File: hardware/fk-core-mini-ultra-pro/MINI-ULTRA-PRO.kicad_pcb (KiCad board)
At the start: 2 copper layers, 25.4 x 55.9 mm, 62 parts, among them J1 S2B-PH-SM4-TB, J2 MICRO-USB, J3 RF-SMA-EDGE, J4 CONN-HDR-1x19, J5 CONN-HDR-1x19, J6 CONN-HDR-2x5, M1 MOUNT_HOLE, M2 MOUNT_HOLE, M3 MOUNT_HOLE, M4 MOUNT_HOLE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

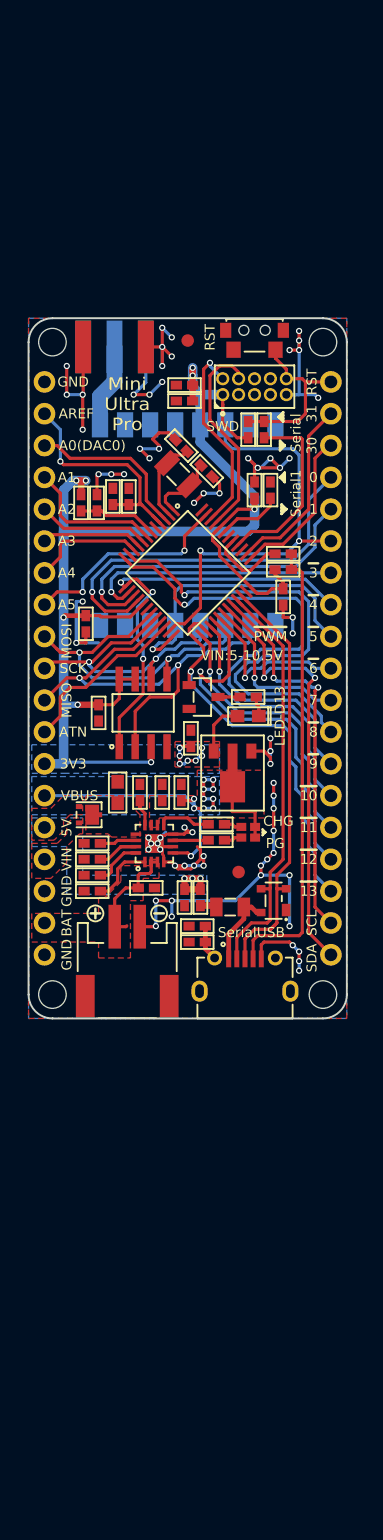
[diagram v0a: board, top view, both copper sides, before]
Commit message: Laying out our additions to the MUP pcb. SD/GPS/Fuel gauge.
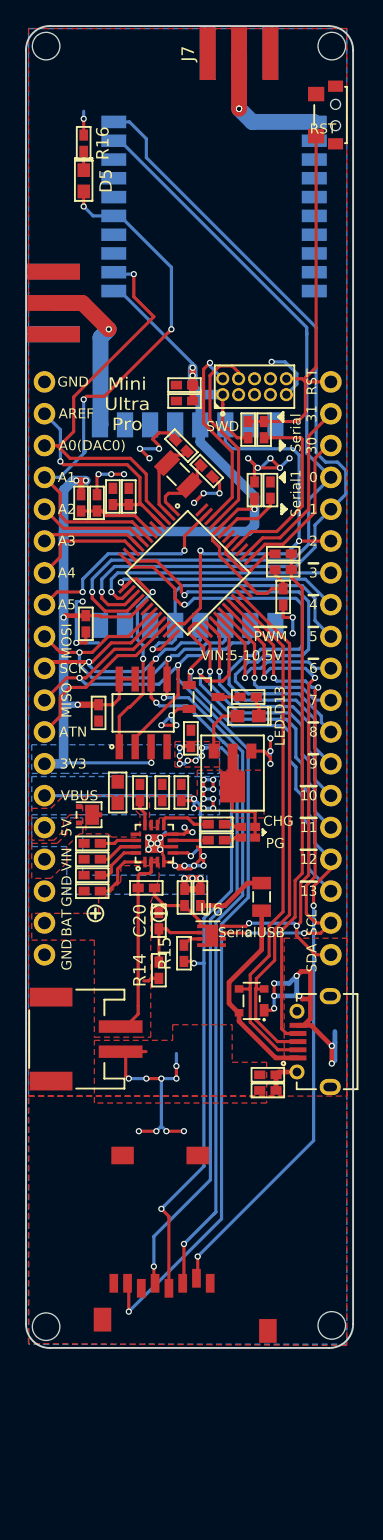
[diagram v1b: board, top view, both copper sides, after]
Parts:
- removed M5, M6: FIDUCIAL, RocketScreamKicadLibrary:FIDUCIAL-1MM
- added C20: 1uF 10V X5R, RocketScreamKicadLibrary:CAP-0402, F.Cu at (137.4, 119.2)
- added D5: Red, RocketScreamKicadLibrary:LED-0603, F.Cu at (131.4, 60.1)
- added J7: RF-SMA-EDGE, RocketScreamKicadLibrary:RF-SMA-EDGE, F.Cu at (143.8, 50.0)
- added M7: MICROSD, microsd:MICROSD, F.Cu at (132.5, 137.5)
- added R14: 1k, RocketScreamKicadLibrary:RES-0402, F.Cu at (137.4, 123.2)
- added R15: 180, RocketScreamKicadLibrary:RES-0402, F.Cu at (139.4, 121.8)
- added R16: 470R, RocketScreamKicadLibrary:RES-0402, F.Cu at (131.4, 57.1)
- added U6: MAX1704XX, Housings_DFN_QFN:DFN-8-1EP_2x2mm_Pitch0.5mm, F.Cu at (141.6, 120.4)
- added U7: FGPMMOPA6H, FGPMMOPA6H:FGPMMOPA6H, B.Cu at (141.8, 62.2)
- J3: moved to F.Cu
- moved M1 26.5 mm to (128.4, 151.6)
- moved M2 26.4 mm to (151.2, 151.5)
- moved M4 23.6 mm to (151.2, 49.4)
- moved M3 23.6 mm to (128.4, 49.4)
- moved SW1 18.2 mm to (151.7, 54.9), turned to 270 degrees
- moved R5 14.3 mm to (146.1, 132.8)
- moved C18 12.0 mm to (146.1, 131.5)
- moved D3 8.19 mm to (144.8, 125.6)
- moved J2 7.67 mm to (149.9, 128.8), turned to 90 degrees
- moved J1 7.03 mm to (131.6, 128.7), turned to 270 degrees
- moved J3 5.99 mm to (129.0, 69.9), turned to 180 degrees
- moved LOGO2 3.06 mm to (136.1, 120.0)
- moved F1 2.64 mm to (145.6, 117.3), turned to 270 degrees
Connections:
- J1 pad 3: Net-(J1-Pad3) -> (no net)
- J1 pad 4: Net-(J1-Pad4) -> (no net)
- J2 pad 7: Net-(J2-Pad7) -> (no net)
- J2 pad 8: Net-(J2-Pad8) -> (no net)
- J2 pad 9: Net-(J2-Pad9) -> (no net)
- J3 pad 2: GND -> (no net)
- J6 pad 6: Net-(J6-Pad6) -> (no net)
- J6 pad 7: Net-(J6-Pad7) -> (no net)
- J6 pad 8: Net-(J6-Pad8) -> (no net)
- U1 pad 39: /TX_LED -> (no net)
- U1 pad 48: /RX_LED -> (no net)
- U3 pad 11: Net-(U3-Pad11) -> (no net)
- U3 pad 12: Net-(U3-Pad12) -> (no net)
- U3 pad 15: Net-(U3-Pad15) -> (no net)
- U3 pad 16: Net-(U3-Pad16) -> (no net)
- U3 pad 6: Net-(U3-Pad6) -> (no net)
- U3 pad 7: Net-(U3-Pad7) -> (no net)
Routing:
- net /MISO: track 37.3 -> 96.4 mm, vias 2 -> 3
- net 3V3: track 130.9 -> 189.9 mm, vias 15 -> 17
- net /SCK: track 23.9 -> 82.3 mm, vias 2 -> 4
- net /MOSI: track 27.5 -> 81.6 mm, vias 2 -> 4
- net /D1: track 26.2 -> 67.1 mm
- net /D12: track 29.3 -> 67.2 mm, vias 1 -> 3
- net /D0: track 30.5 -> 65.0 mm
- net /A1: track 11.2 -> 44.1 mm, vias 0 -> 3
- net /A0: track 13.2 -> 33.6 mm, vias 0 -> 1
- net /RST: track 13.7 -> 31.0 mm
- net Net-(J7-Pad1): track 0.00 -> 10.8 mm, vias 0 -> 2
- net /SCL: track 30.5 -> 40.8 mm, vias 2 -> 4
- net VUSB: track 6.20 -> 16.2 mm
- net GND: track 120.3 -> 111.5 mm, vias 69 -> 55
- net /USB-: track 33.2 -> 41.9 mm
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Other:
- board size 25.4 x 55.9 mm -> 26.1 x 105.5 mm
- net class Default: clearance 0.2032 -> 0.19
- rule trace_clearance: 0.2032 -> 0.19
- rule trace_min: 0.2032 -> 0.19

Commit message: Fixing up edge cuts and consolidating pours.
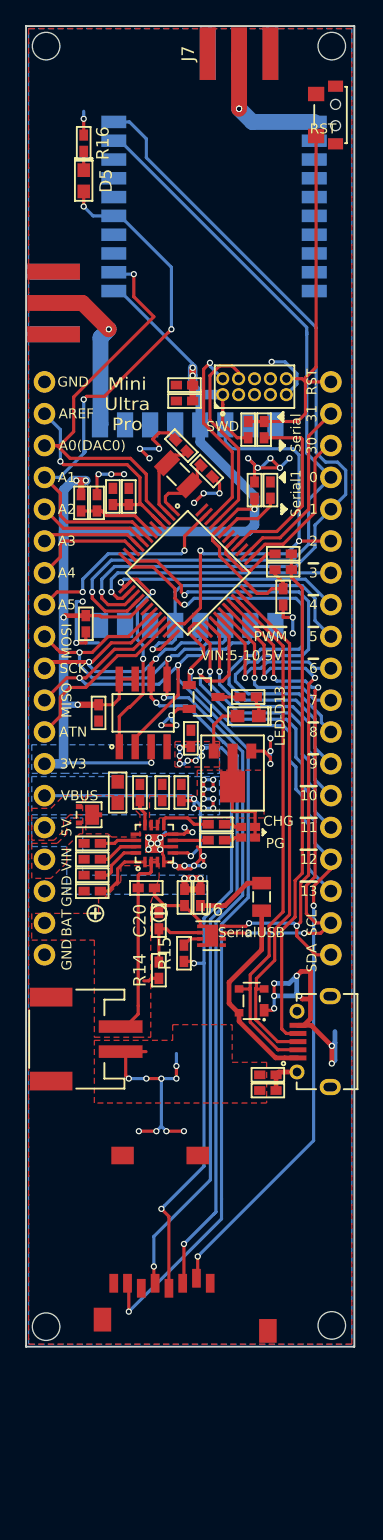
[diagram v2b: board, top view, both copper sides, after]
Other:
- board size 26.1 x 105.5 mm -> 26.2 x 105.4 mm
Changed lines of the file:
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@@
     (links 210)
     (no_connects 0)
-    (area 126.674999 47.744999 152.475001 153.325001)
+    (area 104.521 29.804952 174.451 159.377948)
     (thickness 1.6)
-    (drawings 102)
+    (drawings 98)
     (tracks 1015)
     (zones 0)
@@
     (pad 20 smd rect (at 8.001 6.74878) (size 1.99898 1.00076) (layers B.Cu B.Paste B.Mask))
   )
-  (gr_line (start 126.8 151.4) (end 126.8 49.7) (layer Edge.Cuts) (width 0.15))
-  (gr_line (start 152.9 49.7) (end 152.9 151.4) (layer Edge.Cuts) (width 0.15))
+  (gr_line (start 126.8 153.2) (end 126.8 47.8) (layer Edge.Cuts) (width 0.15))
+  (gr_line (start 153 47.8) (end 153 153.2) (layer Edge.Cuts) (width 0.15))
   (gr_text "Made\nWith" (at 131.572 106.934) (layer B.SilkS)
     (effects (font (size 0.8 0.8) (thickness 0.15)) (justify mirror))
@@
     (effects (font (size 0.8 0.8) (thickness 0.15)))
   )
-  (gr_text RST (at 150.5 56 360) (layer F.SilkS)
+  (gr_text RST (at 150.5 56) (layer F.SilkS)
     (effects (font (size 0.8 0.8) (thickness 0.15)))
   )
@@
   (gr_line (start 131.953 118.618) (end 132.715 118.618) (layer F.SilkS) (width 0.2))
   (gr_line (start 132.334 118.237) (end 132.334 118.999) (layer F.SilkS) (width 0.2))
-  (gr_arc (start 151 151.4) (end 152.905 151.4) (angle 90) (layer Edge.Cuts) (width 0.15))
-  (gr_arc (start 128.7 151.4) (end 128.7 153.305) (angle 90) (layer Edge.Cuts) (width 0.15))
-  (gr_arc (start 150.98 49.73) (end 150.98 47.805) (angle 90.77421614) (layer Edge.Cuts) (width 0.15))
-  (gr_arc (start 128.7 49.7) (end 126.795 49.7) (angle 89.85854995) (layer Edge.Cuts) (width 0.15))
   (gr_text SCL (at 149.606 119.38 90) (layer F.SilkS)
     (effects (font (size 0.8 0.8) (thickness 0.15)))
@@
     (arrow2b (pts (xy 157.35 47.75) (xy 157.936421 48.876504)))
   )
-  (gr_line (start 151 153.3) (end 128.7 153.3) (layer Edge.Cuts) (width 0.15))
-  (gr_line (start 128.7 47.8) (end 151 47.8) (layer Edge.Cuts) (width 0.15))
+  (gr_line (start 153 153.2) (end 126.8 153.2) (layer Edge.Cuts) (width 0.15))
+  (gr_line (start 126.8 47.8) (end 153 47.8) (layer Edge.Cuts) (width 0.15))
   (segment (start 145.376 102.362) (end 145.376 102.87) (width 0.254) (layer F.Cu) (net 1))
   (segment (start 145.376 102.362) (end 145.376 102.108) (width 0.254) (layer F.Cu) (net 1))
@@
     (polygon
       (pts
-        (xy 127 48) (xy 152.4 48) (xy 152.4 153) (xy 127 153)
+        (xy 127 48) (xy 152.8 48) (xy 152.8 153) (xy 127 153)
       )
     )
@@
     (polygon
       (pts
-        (xy 127 48) (xy 127 133.2) (xy 152.4 133.2) (xy 152.4 48)
+        (xy 127 48) (xy 127 153) (xy 152.8 153) (xy 152.8 48)
       )
     )
@@
       )
     )
-  )
-  (zone (net 5) (net_name GND) (layer F.Cu) (hatch edge 0.508)
-    (connect_pads (clearance 0.2032))
-    (min_thickness 0.254)
-    (fill yes (arc_segments 16) (thermal_gap 0.508) (thermal_bridge_width 0.508))
-    (polygon
-      (pts
-        (xy 152.4 153.1) (xy 127 152.95) (xy 127 133.2) (xy 147.4 133.2) (xy 147.4 120.6)
-        (xy 152.4 120.6)
-      )
-    )

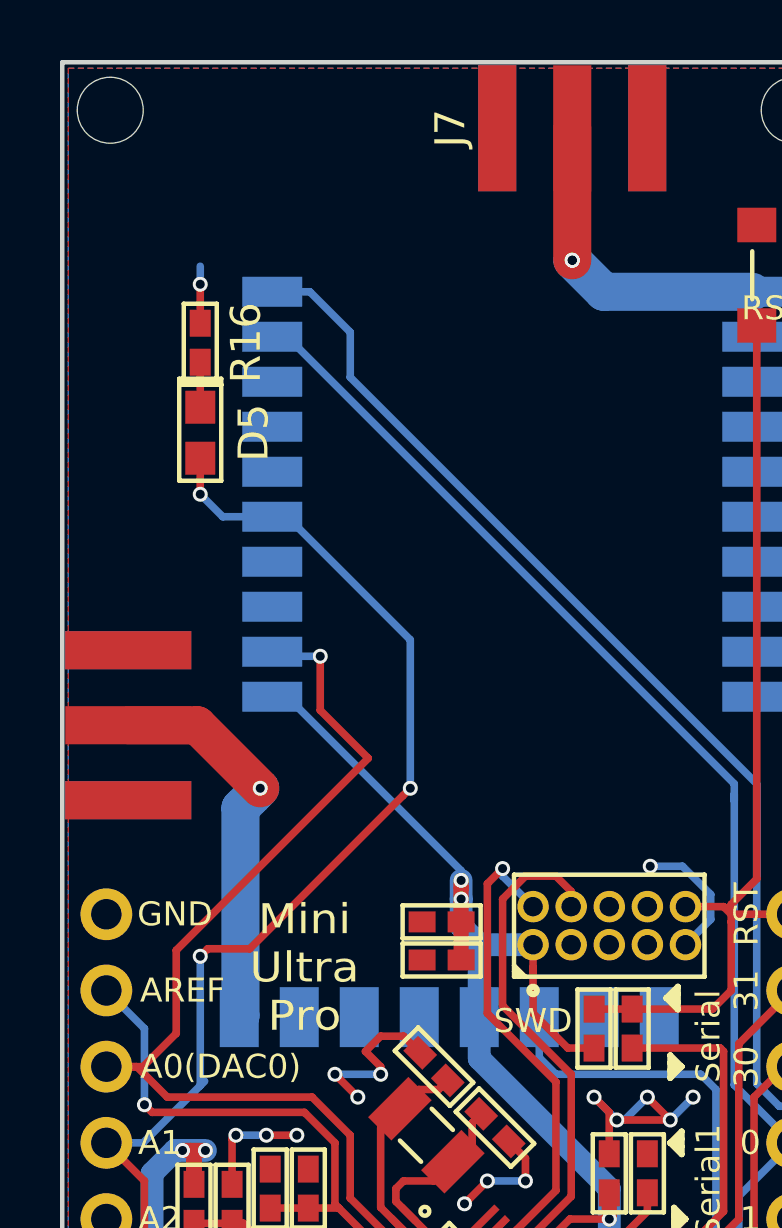
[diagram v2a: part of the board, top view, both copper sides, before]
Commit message: Cleanup silkscreen and some tweaks.
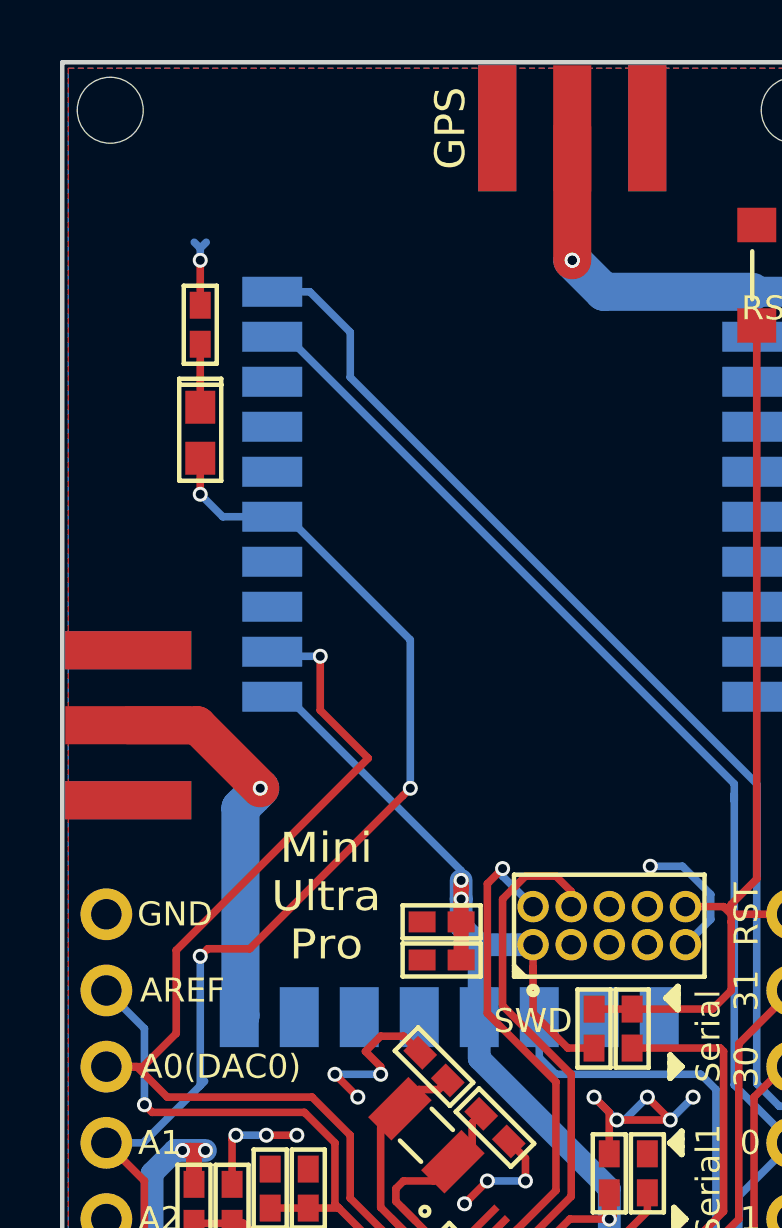
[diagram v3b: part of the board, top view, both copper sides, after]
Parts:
- moved R16 0.60 mm to (131.4, 56.5)
- renumbered J7 to GPS
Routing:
- net Net-(D5-Pad1): track 1.50 -> 2.10 mm
- net GND: track 111.5 -> 112.1 mm
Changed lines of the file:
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@@
     (links 210)
     (no_connects 0)
-    (area 104.521 29.804952 174.451 159.377948)
+    (area 126.724999 47.724999 153.075001 153.275001)
     (thickness 1.6)
     (drawings 98)
-    (tracks 1015)
+    (tracks 1017)
     (zones 0)
     (modules 69)
@@
     (0 F.Cu signal)
     (31 B.Cu signal)
-    (32 B.Adhes user hide)
-    (33 F.Adhes user hide)
-    (34 B.Paste user hide)
-    (35 F.Paste user hide)
+    (32 B.Adhes user)
+    (33 F.Adhes user)
+    (34 B.Paste user)
+    (35 F.Paste user)
     (36 B.SilkS user)
     (37 F.SilkS user)
-    (38 B.Mask user hide)
-    (39 F.Mask user hide)
-    (40 Dwgs.User user)
-    (41 Cmts.User user)
+    (38 B.Mask user)
+    (39 F.Mask user)
+    (40 Dwgs.User user hide)
+    (41 Cmts.User user hide)
     (42 Eco1.User user hide)
     (43 Eco2.User user hide)
     (44 Edge.Cuts user)
     (45 Margin user hide)
-    (46 B.CrtYd user hide)
-    (47 F.CrtYd user hide)
-    (48 B.Fab user)
-    (49 F.Fab user)
+    (46 B.CrtYd user)
+    (47 F.CrtYd user)
+    (48 B.Fab user hide)
+    (49 F.Fab user hide)
   )
   (setup
@@
     (aux_axis_origin 127 127)
     (grid_origin 127 127)
-    (visible_elements 7FFCDF19)
+    (visible_elements 7FFFDF7F)
     (pcbplotparams
       (layerselection 0x010fc_80000001)
@@
     (tags "LED led 0603 SMD smd SMT smt smdled SMDLED smtled SMTLED")
     (attr smd)
-    (fp_text reference D5 (at 0 -1.778 270) (layer F.SilkS)
+    (fp_text reference D5 (at 0 -1.778 270) (layer F.SilkS) hide
       (effects (font (size 1 1) (thickness 0.15)))
     )
@@
   (module RocketScreamKicadLibrary:RF-SMA-EDGE (layer F.Cu)
     (at 143.8 50 90)
-    (fp_text reference J7 (at 0 -4.064 90) (layer F.SilkS)
+    (fp_text reference GPS (at 0 -4.064 90) (layer F.SilkS)
       (effects (font (size 1 1) (thickness 0.15)))
     )
@@
   )
   (module RocketScreamKicadLibrary:RES-0402 (layer F.Cu)
-    (at 131.4 57.15 270)
-    (fp_text reference R16 (at 0 -1.524 270) (layer F.SilkS)
+    (at 131.4 56.55 270)
+    (fp_text reference R16 (at 0 -1.524 270) (layer F.SilkS) hide
       (effects (font (size 1 1) (thickness 0.15)))
     )
@@
   (module FGPMMOPA6H:FGPMMOPA6H (layer B.Cu)
     (at 141.8 62.2)
-    (fp_text reference U7 (at -1.00076 -8.99922) (layer B.SilkS)
+    (fp_text reference U7 (at 0 -0.4) (layer B.SilkS) hide
       (effects (font (thickness 0.3048)) (justify mirror))
     )
-    (fp_text value FGPMMOPA6H (at 0 8.99922) (layer B.SilkS)
+    (fp_text value FGPMMOPA6H (at 0 8.99922) (layer B.SilkS) hide
       (effects (font (thickness 0.3048)) (justify mirror))
     )
-    (fp_text user 1 (at -5.3848 6.5024) (layer B.SilkS)
+    (fp_text user 1 (at -5.3848 6.5024) (layer B.SilkS) hide
       (effects (font (thickness 0.3048)) (justify mirror))
     )
@@
     (effects (font (size 0.8 0.8) (thickness 0.15)))
   )
-  (gr_text "Mini \nUltra Pro\n11-2015 \n0v20" (at 144.2085 124.206) (layer B.SilkS)
+  (gr_text "Mini \nUltra Pro\n11-2015 \n0v20" (at 139.8 128) (layer B.SilkS)
     (effects (font (size 0.8 0.8) (thickness 0.15)) (justify mirror))
   )
@@
     (effects (font (size 0.8 0.8) (thickness 0.15)))
   )
-  (gr_text "Mini\nUltra\nPro" (at 134.874 77.978) (layer F.SilkS)
+  (gr_text "Mini\nUltra\nPro" (at 135.6 75.6) (layer F.SilkS)
     (effects (font (size 1 1.1) (thickness 0.2)))
   )
@@
   (segment (start 132.7 79.63) (end 132.739939 79.590061) (width 1.27) (layer B.Cu) (net 4))
   (via (at 133.4 72) (size 0.5) (drill 0.3) (layers F.Cu B.Cu) (net 4))
+  (segment (start 131.4 54) (end 131.2 53.8) (width 0.254) (layer B.Cu) (net 5))
+  (segment (start 131.4 54) (end 131.6 53.8) (width 0.254) (layer B.Cu) (net 5))
+  (segment (start 131.4 54.4) (end 131.4 54) (width 0.254) (layer B.Cu) (net 5))
+  (segment (start 131.4 55.9) (end 131.4 54.4) (width 0.254) (layer F.Cu) (net 5))
+  (via (at 131.4 54.4) (size 0.5) (drill 0.3) (layers F.Cu B.Cu) (net 5))
   (segment (start 138.4 102.8) (end 138.4 103.2) (width 0.254) (layer B.Cu) (net 5))
   (segment (start 138.4 103.2) (end 138.8 103.6) (width 0.254) (layer B.Cu) (net 5))
@@
   (segment (start 148.416001 76.373999) (end 148.416001 75.541839) (width 0.254) (layer B.Cu) (net 5))
   (segment (start 148.416001 75.541839) (end 147.474162 74.6) (width 0.254) (layer B.Cu) (net 5))
-  (segment (start 131.4 55.2) (end 131.4 54.6) (width 0.254) (layer B.Cu) (net 5))
-  (segment (start 131.4 56.5) (end 131.4 55.2) (width 0.254) (layer F.Cu) (net 5))
-  (via (at 131.4 55.2) (size 0.5) (drill 0.3) (layers F.Cu B.Cu) (net 5))
   (segment (start 149.5 127.025) (end 149.5 125.4) (width 0.381) (layer F.Cu) (net 5))
   (segment (start 149.5 125.4) (end 149.5 123.25) (width 0.381) (layer F.Cu) (net 5))
@@
   (segment (start 138.304 120.15) (end 140.196 120.15) (width 0.254) (layer F.Cu) (net 64))
   (segment (start 140.196 120.15) (end 140.7 120.15) (width 0.254) (layer F.Cu) (net 64))
-  (segment (start 131.4 59.3) (end 131.4 57.8) (width 0.254) (layer F.Cu) (net 65))
+  (segment (start 131.4 59.3) (end 131.4 57.2) (width 0.254) (layer F.Cu) (net 65))
   (segment (start 143.8 54.4) (end 143.8 50) (width 1.27) (layer F.Cu) (net 66))
   (via (at 143.8 54.4) (size 0.5) (drill 0.3) (layers F.Cu B.Cu) (net 66))

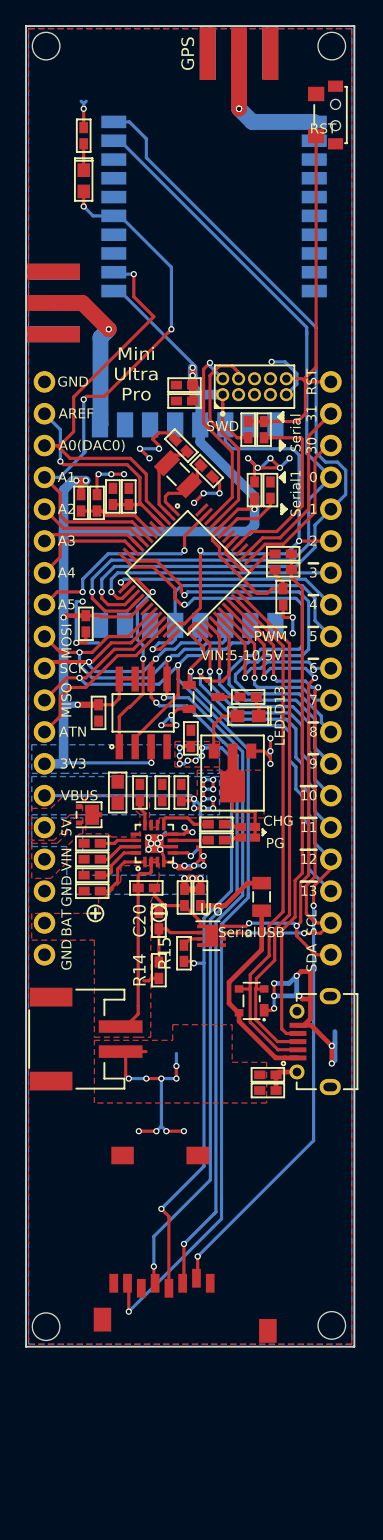
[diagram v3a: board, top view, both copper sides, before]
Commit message: Better routing of SDA/SCL and some other cleanup.
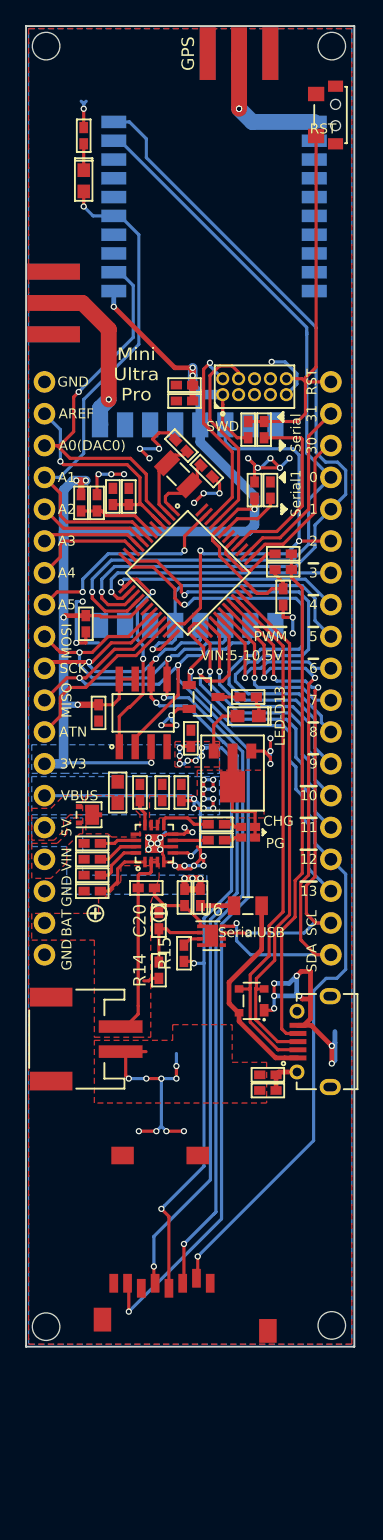
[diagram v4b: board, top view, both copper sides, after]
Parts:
- moved F1 1.30 mm to (144.5, 118.0), turned to 0 degrees
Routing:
- net /SDA: track 42.1 -> 46.4 mm, vias 4 -> 3
- net /A1: track 44.1 -> 40.9 mm, vias 3 -> 1
- net Net-(F1-Pad1): track 5.63 -> 2.69 mm
- net /D12: track 67.2 -> 69.4 mm, vias 3 -> 2
- net /A0: track 33.6 -> 31.9 mm
- net 3V3: track 189.9 -> 190.9 mm, vias 17 -> 18
- net /SCL: vias 4 -> 3
